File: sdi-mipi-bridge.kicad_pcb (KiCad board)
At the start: 6 copper layers, 70 x 42 mm, 202 parts, among them J1 031-70526-21, J2 031-70526-21, J3 WE_68715014522_ONE-SIDE, J4 2199SB-10G-301523, J5 MC-HVT1-S04-G, J6 2199SB-10G-301523, SW1 SW_DIP_x06, SW2 SW_DIP_x06, U1 MAX8902B, U2 GS2971A, U3 GS2988, U4 CrossLink_LIF-MD6000-6JMG80I, U5 SC18IS602BIPW, Y1 ABM7_27.000MH_D2Y_T

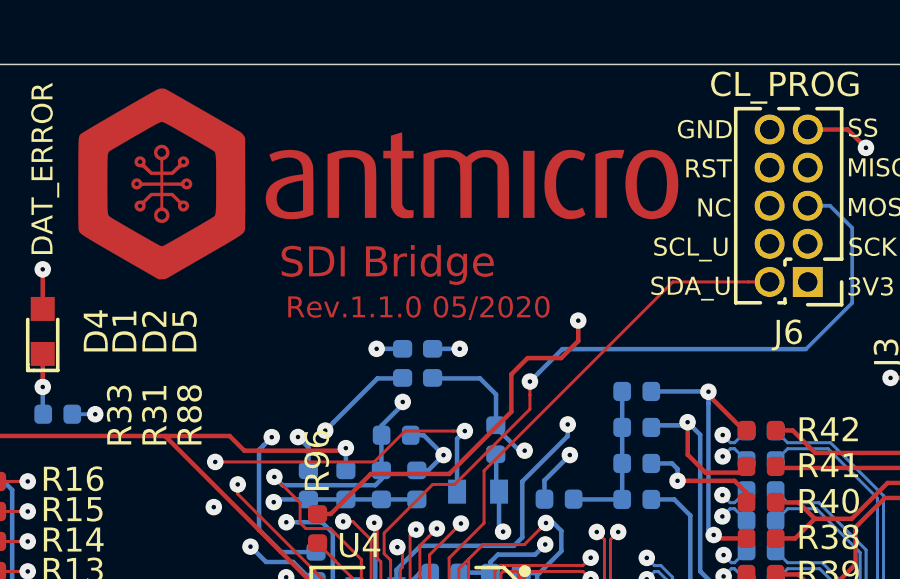
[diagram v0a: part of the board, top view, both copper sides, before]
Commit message: Update naming convention
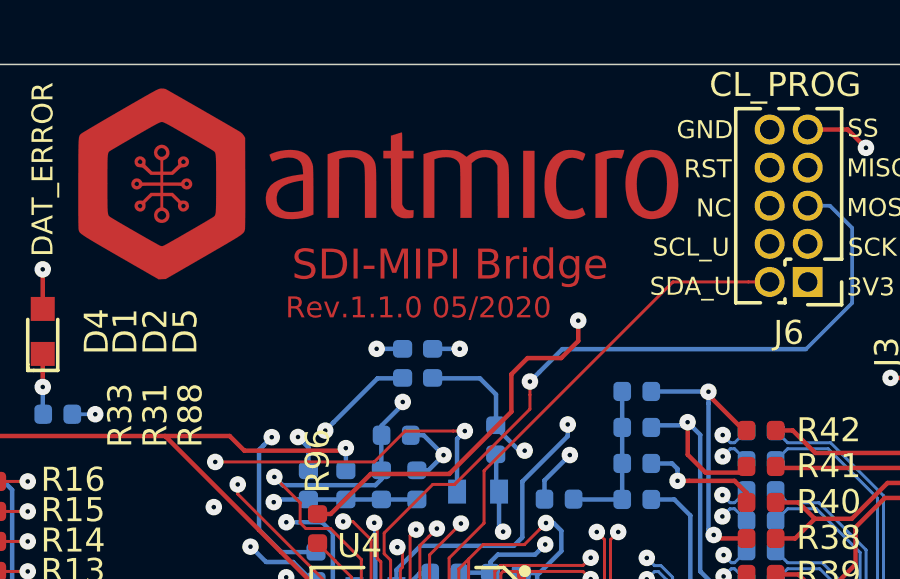
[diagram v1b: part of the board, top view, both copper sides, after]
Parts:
- C1, C15, C58: footprint SDI-bridge-footprints:0603-cap -> sdi-mipi-bridge-footprints:0603-cap
- C10, C11, C12, C13, C14, C16, C17, C18, C19, C2, C20, C21, C22, C23, C24, C25, C26, C28, C29, C3, C30, C31, C32, C33, C34, C35, C36, C37, C38, C39, C4, C40, C41, C42, C44, C45, C46, C47, C48, C49, C5, C50, C51, C52, C53, C54, C55, C56, C57, C6, C61, C62, C63, C64, C65, C7, C8, C9: footprint SDI-bridge-footprints:0402-cap -> sdi-mipi-bridge-footprints:0402-cap
- C27, C59, C60, R1, R10, R11, R12, R13, R14, R15, R16, R2, R21, R22, R23, R24, R25, R26, R29, R3, R30, R31, R32, R33, R34, R35, R36, R37, R38, R39, R4, R40, R41, R42, R43, R44, R45, R46, R47, R48, R49, R5, R50, R51, R52, R53, R54, R55, R56, R57, R58, R59, R6, R60, R61, R62, R63, R64, R67, R69, R7, R70, R71, R72, R73, R74, R8, R88, R89, R9, R90, R91, R93, R95: footprint SDI-bridge-footprints:0402-res -> sdi-mipi-bridge-footprints:0402-res
- C43, FB1, FB2, FB3, R17, R18, R19, R20, R27, R28: footprint SDI-bridge-footprints:0603-res -> sdi-mipi-bridge-footprints:0603-res
- D1, D2, D4, D5: footprint SDI-bridge-footprints:LED_0603 -> sdi-mipi-bridge-footprints:LED_0603
- J1, J2: footprint SDI-bridge-footprints:BNC_Edge_Conn -> sdi-mipi-bridge-footprints:BNC_Edge_Conn
- J3: footprint SDI-bridge-footprints:WE_68715014522_ONE-SIDE -> sdi-mipi-bridge-footprints:WE_68715014522_ONE-SIDE
- J4, J6: footprint antmicro-footprints:PinHeader_2x05_P1.27mm_Vertical -> sdi-mipi-bridge-footprints:PinHeader_2x05_P1.27mm_Vertical
- J5: footprint SDI-bridge-footprints:PinHeader_1x4_P1.27mm_Drill.7mm -> sdi-mipi-bridge-footprints:PinHeader_1x4_P1.27mm_Drill.7mm
- N1: footprint SDI-bridge-footprints:antmicro-logo_scaled_20mm -> sdi-mipi-bridge-footprints:antmicro-logo_scaled_20mm
- N2: footprint antmicro-footprints:oshw-logo -> sdi-mipi-bridge-footprints:oshw-logo
- R65, R66, R68, R75, R76, R77, R78, R79, R80, R81, R82, R83, R84, R85, R86, R87, R94, R96: footprint antmicro-footprints:0402-res -> sdi-mipi-bridge-footprints:0402-res
- S1: footprint antmicro-footprints:Switch_Tactile_SMD_B3U-1000P -> sdi-mipi-bridge-footprints:Switch_Tactile_SMD_B3U-1000P
- SW1, SW2: footprint antmicro-footprints:SW_SPST_6_Slide_MCDHN-06F-T-V_P1.27mm -> sdi-mipi-bridge-footprints:SW_SPST_6_Slide_MCDHN-06F-T-V_P1.27mm
- TP1, TP17, TP18, TP19, TP2, TP20, TP21, TP6: footprint SDI-bridge-footprints:Testpoint_smd_1mm -> sdi-mipi-bridge-footprints:Testpoint_smd_1mm
- TP10, TP11, TP12, TP13, TP14, TP15, TP16, TP7, TP8, TP9: footprint SDI-bridge-footprints:Testpoint_smd_0_75mm -> sdi-mipi-bridge-footprints:Testpoint_smd_0_75mm
- U1: footprint SDI-bridge-footprints:TDFN2x2 -> sdi-mipi-bridge-footprints:TDFN2x2
- U2: footprint SDI-bridge-footprints:BGA100_11x11mm -> sdi-mipi-bridge-footprints:BGA100_11x11mm
- U3: footprint SDI-bridge-footprints:QFN-16_EP_4x4_Pitch0.65mm -> sdi-mipi-bridge-footprints:QFN-16_EP_4x4_Pitch0.65mm
- U4: footprint SDI-bridge-footprints:BGA-80pin_ckfBGA80_7.0x7.0mm -> sdi-mipi-bridge-footprints:BGA-80pin_ckfBGA80_7.0x7.0mm
- U5: footprint SDI-bridge-footprints:SC18IS602B -> sdi-mipi-bridge-footprints:SC18IS602B
- Y1: footprint SDI-bridge-footprints:ABM7_OSC -> sdi-mipi-bridge-footprints:ABM7_OSC
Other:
- board text added: "SDI-MIPI Bridge"
- board text removed: "SDI Bridge"

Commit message: Add stackup table to the PCB fab layer
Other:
- board text added: "0.018 mm"
- board text added: "0.02 mm"
- board text added: "0.035 mm"
- board text added: "0.12 mm"
- board text added: "0.36 mm"
- board text added: "1"
- board text added: "10"
- board text added: "11"
- board text added: "12"
- board text added: "13"
- board text added: "14"
- board text added: "15"
- board text added: "16"
- board text added: "2"
- board text added: "3"
- board text added: "3.5"
- board text added: "4"
- board text added: "4.2"
- board text added: "5"
- board text added: "6"
- board text added: "7"
- board text added: "8"
- board text added: "9"
- board text added: "Bottom Layer"
- board text added: "Bottom Solder"
- board text added: "Constant"
- board text added: "Copper"
- board text added: "Dielectric 1"
- board text added: "Dielectric 2"
- board text added: "Dielectric 3"
- board text added: "Dielectric 4"
- board text added: "Dielectric 5"
- board text added: "Dielectric 6"
- board text added: "Dielectric 7"
- board text added: "Dielectric 8"
- board text added: "FR-4"
- board text added: "Gold plating (ENIG, selective)"
- board text added: "Layer"
- board text added: "Material"
- board text added: "Name"
- board text added: "Power Plane 1"
- board text added: "Power Plane 2"
- board text added: "Prepreg"
- board text added: "Recommended PCB finish:"
- board text added: "Recommended PCB stackup"
- board text added: "Signal 1"
- board text added: "Signal 2"
- board text added: "Silkscreen: white"
- board text added: "Solder Resist"
- board text added: "Solder mask: matt black"
- board text added: "Suggested prepreg material is ISOLA PR2116"
- board text added: "The design includes high speed signaling"
- board text added: "Thickness"
- board text added: "Top Layer"
- board text added: "Top Solder"

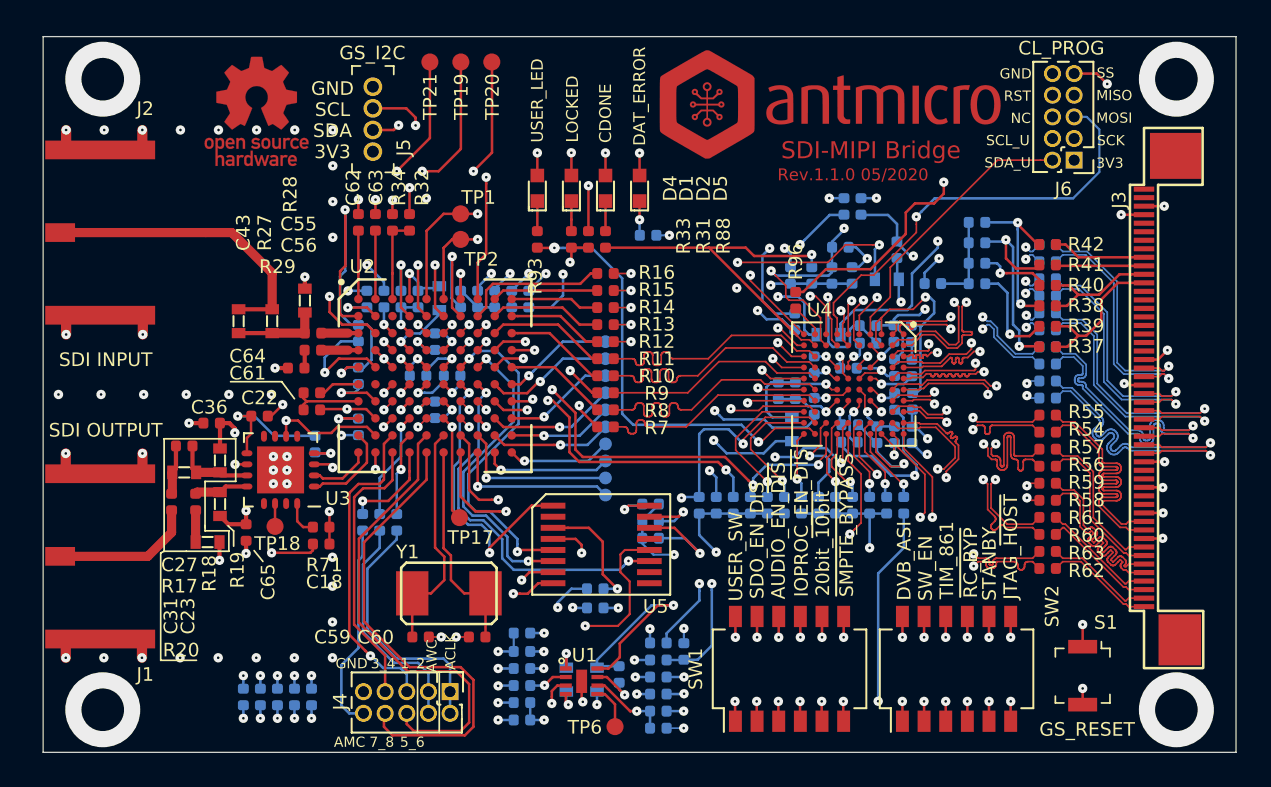
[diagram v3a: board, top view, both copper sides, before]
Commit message: Update 3D model of the BNC connector
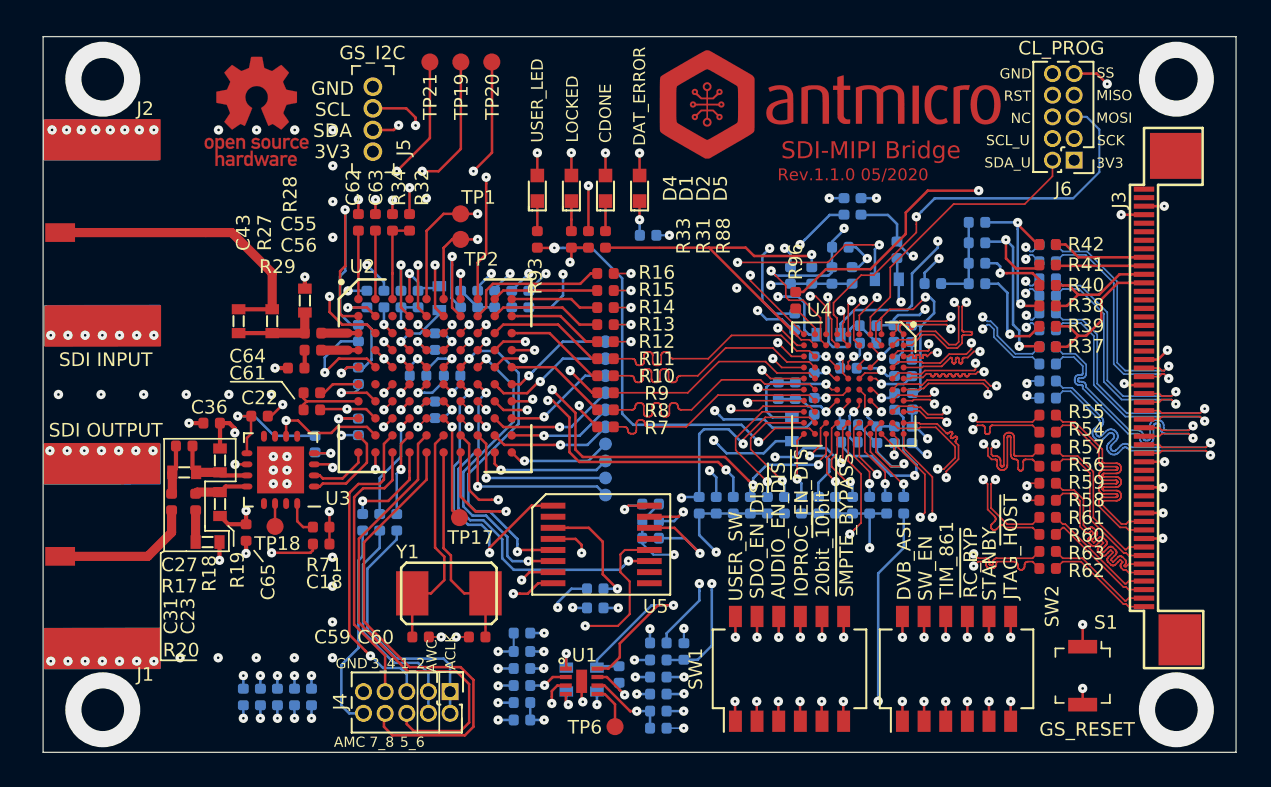
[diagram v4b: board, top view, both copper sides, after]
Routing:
- net /USER_SDA: track 16.5 -> 17.1 mm
- net GNDA: vias 73 -> 91

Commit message: Change C37 from 2n2 to 2u2
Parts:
- C37: value C_2n2_0402 -> C_2u2_0402

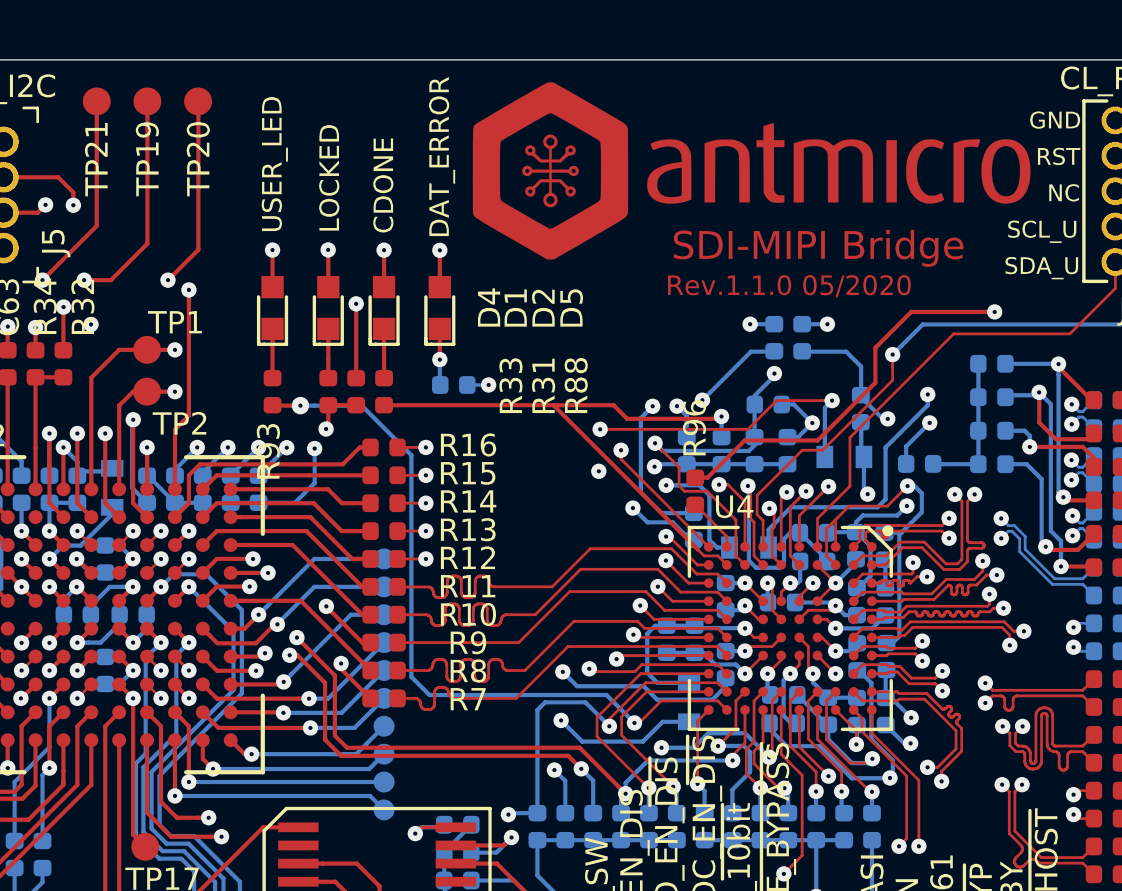
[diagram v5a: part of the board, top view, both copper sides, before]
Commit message: Add changes to PCB
Connect PCLK signal to J7 pin of FPGA
Replace DOUT10 and DOUT11 resistors with test pads
Add second user LED indicator
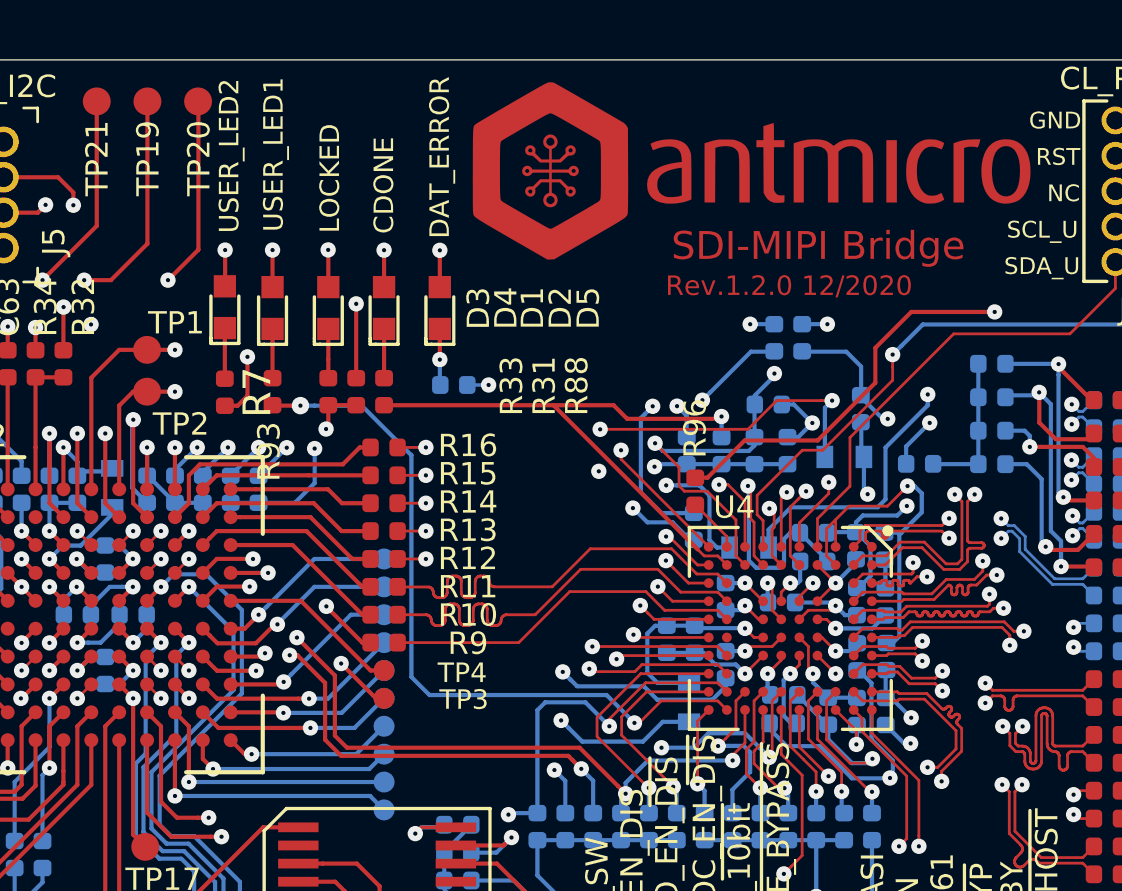
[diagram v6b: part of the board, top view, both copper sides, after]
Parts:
- removed R8: R_0R_0402, sdi-mipi-bridge-footprints:0402-res
- added D3: LG_L29K-G2J1-24-Z, sdi-mipi-bridge-footprints:LED_0603, F.Cu at (125.3, 104.4)
- added TP3: TP_SMD_0_75MM, sdi-mipi-bridge-footprints:Testpoint_smd_0_75mm, F.Cu at (131.1, 118.4)
- added TP4: TP_SMD_0_75MM, sdi-mipi-bridge-footprints:Testpoint_smd_0_75mm, F.Cu at (131.1, 117.4)
- FB1, FB2, FB3: value BLM18PG121SN1D -> BLM18PG121SH1D
- J1, J2: value 031-70526-21 -> 112740-13
- J4, J6: value 2199SB-10G-301523 -> GRPB052VWVN-RC
- J5: value MC-HVT1-S04-G -> GRPB041VWVN-RC
- R7: value R_0R_0402 -> R_100R_0402
- moved R7 12.4 mm to (125.3, 107.4), turned to 270 degrees
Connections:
- net /USER_LED renamed /USER_LED1
- R7 pad 1: /DOUT10 -> Net-(D3-Pad1)
- R7 pad 2: /D10 -> /USER_LED2
- U2 pad E10: /D11 -> Net-(TP4-Pad1)
- U2 pad E9: /D10 -> Net-(TP3-Pad1)
- U4 pad E1: /PCLK -> /USER_LED2
- U4 pad J6: /DOUT11 -> Net-(U4-PadJ6)
- U4 pad J7: /DOUT10 -> /PCLK
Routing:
- net /USER_LED2: track 0.00 -> 31.3 mm, vias 0 -> 2
- net /DOUT11: track 15.7 -> 0.00 mm
- net /DOUT10: track 13.8 -> 0.00 mm
- net /PCLK: track 36.4 -> 24.5 mm
- net Net-(TP3-Pad1): track 0.00 -> 8.37 mm, vias 0 -> 2
- net /D10: track 8.00 -> 0.00 mm, vias 2 -> 0
- net Net-(TP4-Pad1): track 0.00 -> 6.53 mm
- net /D11: track 6.05 -> 0.00 mm
- net Net-(D3-Pad1): track 0.00 -> 1.81 mm
- net GNDREF: track 119.5 -> 120.9 mm, vias 51 -> 52
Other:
- board text added: "Rev.1.2.0 12/2020"
- board text added: "USER_LED1"
- board text added: "USER_LED2"
- board text removed: "Rev.1.1.0 05/2020"
- board text removed: "USER_LED"
